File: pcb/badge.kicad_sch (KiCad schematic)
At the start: 17 parts, among them J1 USB_C_Receptacle_USB2.0_16P, U1 ESP32-C3-WROOM-02, U2 AMS1117-3.3

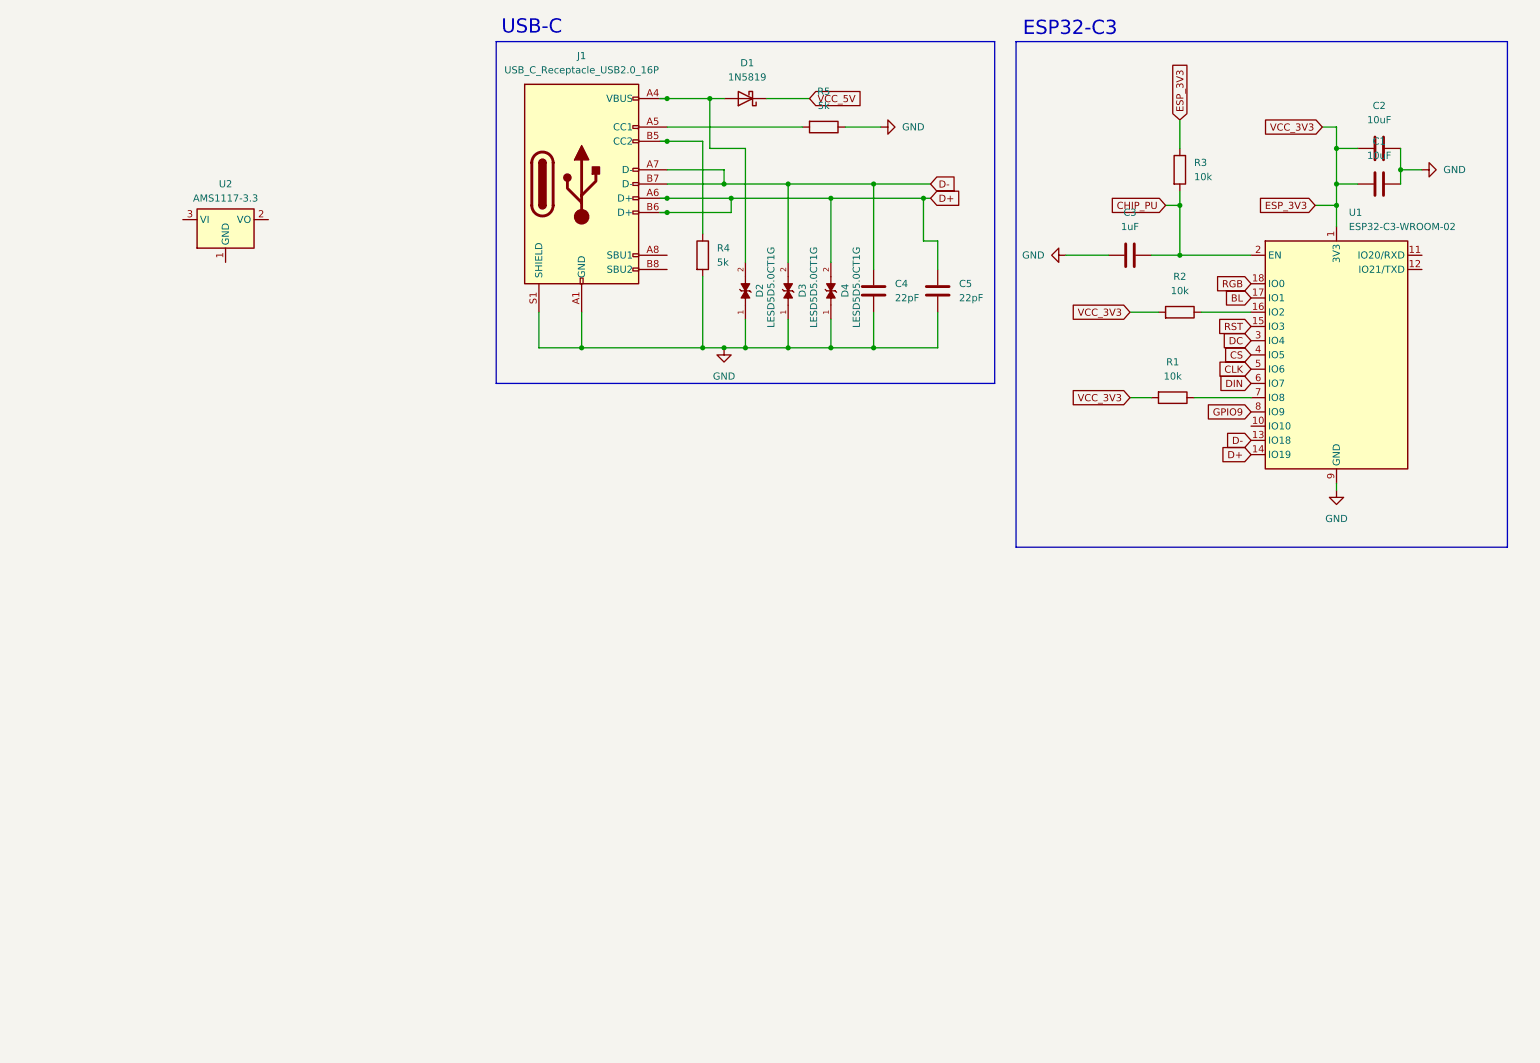
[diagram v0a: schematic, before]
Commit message: Made symbol for GDEY0213F51
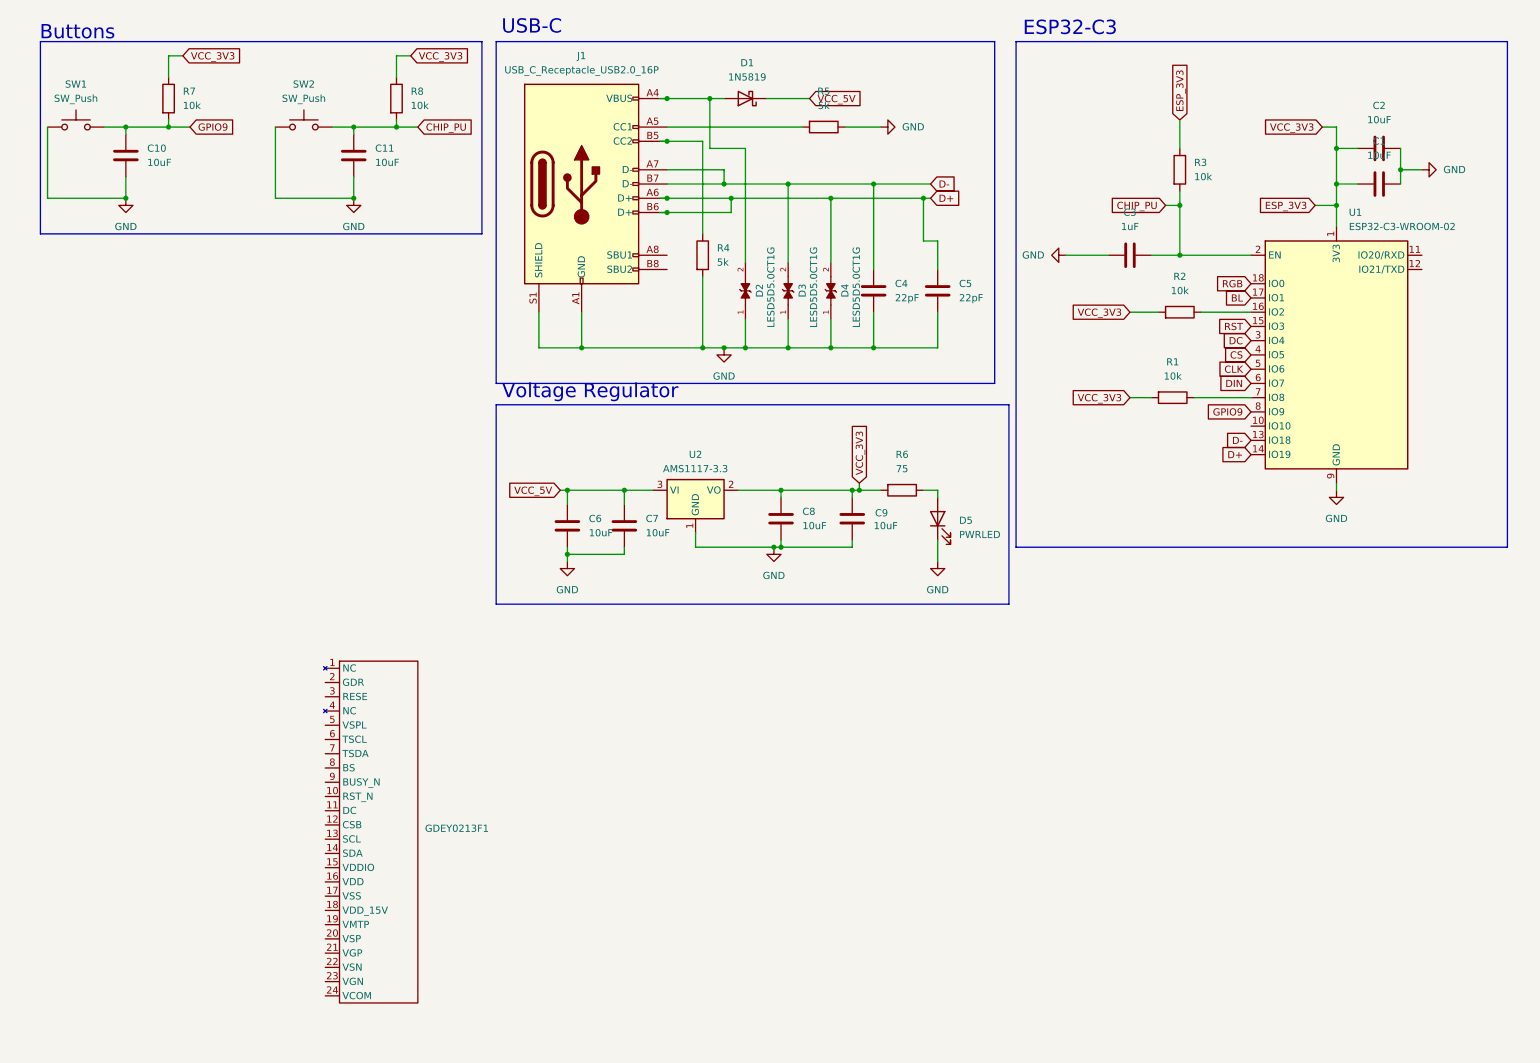
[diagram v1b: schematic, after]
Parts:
- added C10, C11, C6, C7, C8, C9: 10uF, symbol Device:C
- added D5: PWRLED, symbol Device:LED
- added GDEY0213F1: ~, symbol GDEY0213F51:GDEY0213F51
- added R6: 75, symbol Device:R
- added R7, R8: 10k, symbol Device:R
- added SW1, SW2: SW_Push, symbol Switch:SW_Push
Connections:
- net CHIP_PU: now also C11.1, R8.2, SW2.2
- net ESP_3V3: now also U2.2 (VO), C8.1, C9.1, R6.2, R7.1, R8.1
- net GND: now also U2.1 (GND), C10.2, C11.2, C6.2, C7.2, C8.2, C9.2, D5.1 (K), SW1.1, SW2.1
- net GPIO9: now also C10.1, R7.2, SW1.2
- net VCC_5V: now also U2.3 (VI), C6.1, C7.1
- new net: D5.2 (A), R6.1
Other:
- note added: "Buttons"
- note added: "Voltage Regulator"
- moved on the sheet: U2

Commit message: Began changing to rp2040
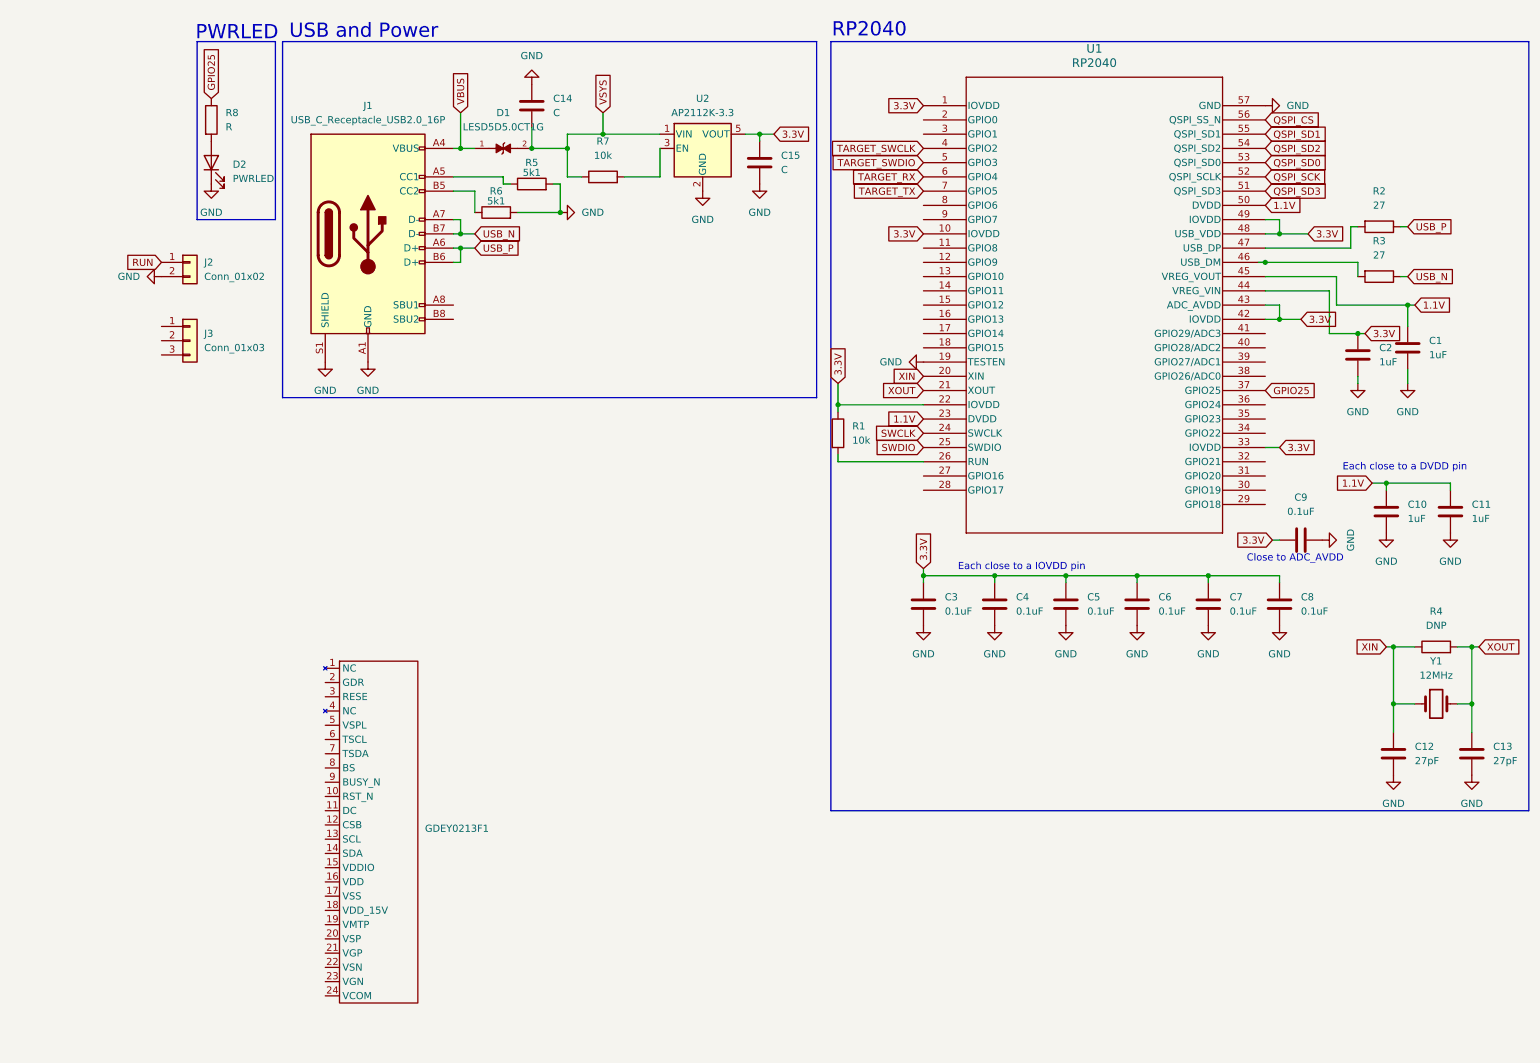
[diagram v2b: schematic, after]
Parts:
- removed D1: 1N5819, Diode_THT:D_DO-41_SOD81_P10.16mm_Horizontal, symbol Diode:1N5819
- removed D2, D3, D4: LESD5D5.0CT1G, LESD5D5.0CT1G:TVS_LESD5D5.0CT1G, symbol LESD5D5.0CT1G:LESD5D5.0CT1G
- removed D5: PWRLED, symbol Device:LED
- removed SW1, SW2: SW_Push, symbol Switch:SW_Push
- removed U1: ESP32-C3-WROOM-02, RF_Module:ESP32-C3-WROOM-02, symbol RF_Module:ESP32-C3-WROOM-02
- removed U2: AMS1117-3.3, Package_TO_SOT_SMD:SOT-223-3_TabPin2, symbol Regulator_Linear:AMS1117-3.3
- added C12, C13: 27pF, symbol Device:C
- added C14, C15: C, symbol Device:C
- added D1: LESD5D5.0CT1G, LESD5D5.0CT1G:TVS_LESD5D5.0CT1G, symbol LESD5D5.0CT1G:LESD5D5.0CT1G
- added D2: PWRLED, symbol Device:LED
- added J2: Conn_01x02, symbol Connector_Generic:Conn_01x02
- added J3: Conn_01x03, symbol Connector_Generic:Conn_01x03
- added U1: RP2040, IC57_RP2040, symbol RP2040:RP2040
- added U2: AP2112K-3.3, Package_TO_SOT_SMD:SOT-23-5, symbol Regulator_Linear:AP2112K-3.3
- added Y1: 12MHz, symbol Device:Crystal
- C1, C10, C11, C2: value 10uF -> 1uF
- C3: value 1uF -> 0.1uF
- C4, C5: value 22pF -> 0.1uF
- C6, C7, C8, C9: value 10uF -> 0.1uF
- R2, R3: value 10k -> 27
- R4: value 5k -> DNP
- R5: value 5k -> 5k1
- R6: value 75 -> 5k1
- R8: value 10k -> R
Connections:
- net VCC_5V is gone; now on net 3.3V: C6.1, C7.1
- net GND: now also C1.2, C3.2, R5.2, R6.2, C12.2, C13.2, C14.1, C15.2, D2.1 (K), J2.2 (Pin_2), U1.19 (TESTEN), U1.57 (GND), U2.2 (GND); no longer C1.1, C3.1, R4.2, R5.1
- net at J1.A5 (CC1): now also R5.1; no longer R5.2
- net VBUS: now reaches J1.A4 (VBUS), J1.A9 (VBUS), J1.B4 (VBUS), J1.B9 (VBUS)
- net VBUS: now also D1.1
- net at R6.1: now also J1.B5 (CC2)
- net XIN: now reaches R4.1
- net XIN: now also C12.1, U1.20 (XIN), Y1.1; no longer J1.B5 (CC2)
- net 3.3V: now reaches R1.1
- net 3.3V: now also C2.1, C3.1, C4.1, C5.1, C8.1, C9.1, C15.1, U1.1 (IOVDD), U1.10 (IOVDD), U1.22 (IOVDD), U1.33 (IOVDD), U1.42 (IOVDD), U1.43 (ADC_AVDD), U1.44 (VREG_VIN), U1.48 (USB_VDD), U1.49 (IOVDD), U2.5 (VOUT)
- net USB_P: now reaches R2.1
- net USB_P: now also J1.A6 (D+), J1.B6 (D+)
- removed net CHIP_PU: C11.1, C3.2, R3.2, R8.2
- removed net D+: C5.1, J1.A6 (D+), J1.B6 (D+)
- net D- renamed USB_N
- net USB_N: now also R3.1; no longer C4.1
- removed net ESP_3V3: C1.2, C2.1, C8.1, C9.1, R1.2, R2.2, R3.1, R6.2, R7.1, R8.1
- net GPIO9: no longer names the net of R7.2
- net GPIO9: now also U2.3 (EN); no longer C10.1
- new net: R1.2, U1.26 (RUN)
- new net: R3.2, U1.46 (USB_DM)
- new net: R2.2, U1.47 (USB_DP)
- new net: D2.2 (A), R8.2
- new net 1.1V: C1.1, C10.1, C11.1, U1.23 (DVDD), U1.45 (VREG_VOUT), U1.50 (DVDD)
- new net GPIO25: R8.1, U1.37 (GPIO25)
- new net QSPI_CS: U1.56 (QSPI_SS_N)
- new net QSPI_SCK: U1.52 (QSPI_SCLK)
- new net QSPI_SD0: U1.53 (QSPI_SD0)
- new net QSPI_SD1: U1.55 (QSPI_SD1)
- new net QSPI_SD2: U1.54 (QSPI_SD2)
- new net QSPI_SD3: U1.51 (QSPI_SD3)
- new net RUN: J2.1 (Pin_1)
- new net SWCLK: U1.24 (SWCLK)
- new net SWDIO: U1.25 (SWDIO)
- new net TARGET_RX: U1.6 (GPIO4)
- new net TARGET_SWCLK: U1.4 (GPIO2)
- new net TARGET_SWDIO: U1.5 (GPIO3)
- new net TARGET_TX: U1.7 (GPIO5)
- new net VSYS: C14.2, D1.2, R7.1, U2.1 (VIN)
- new net XOUT: C13.1, R4.2, U1.21 (XOUT), Y1.2
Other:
- note added: "Close to ADC_AVDD"
- note added: "Each close to a DVDD pin"
- note added: "Each close to a IOVDD pin"
- note added: "PWRLED"
- note added: "RP2040"
- note added: "USB and Power"
- note removed: "Buttons"
- note removed: "ESP32-C3"
- note removed: "USB-C"
- note removed: "Voltage Regulator"

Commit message: Beginning to get footprints
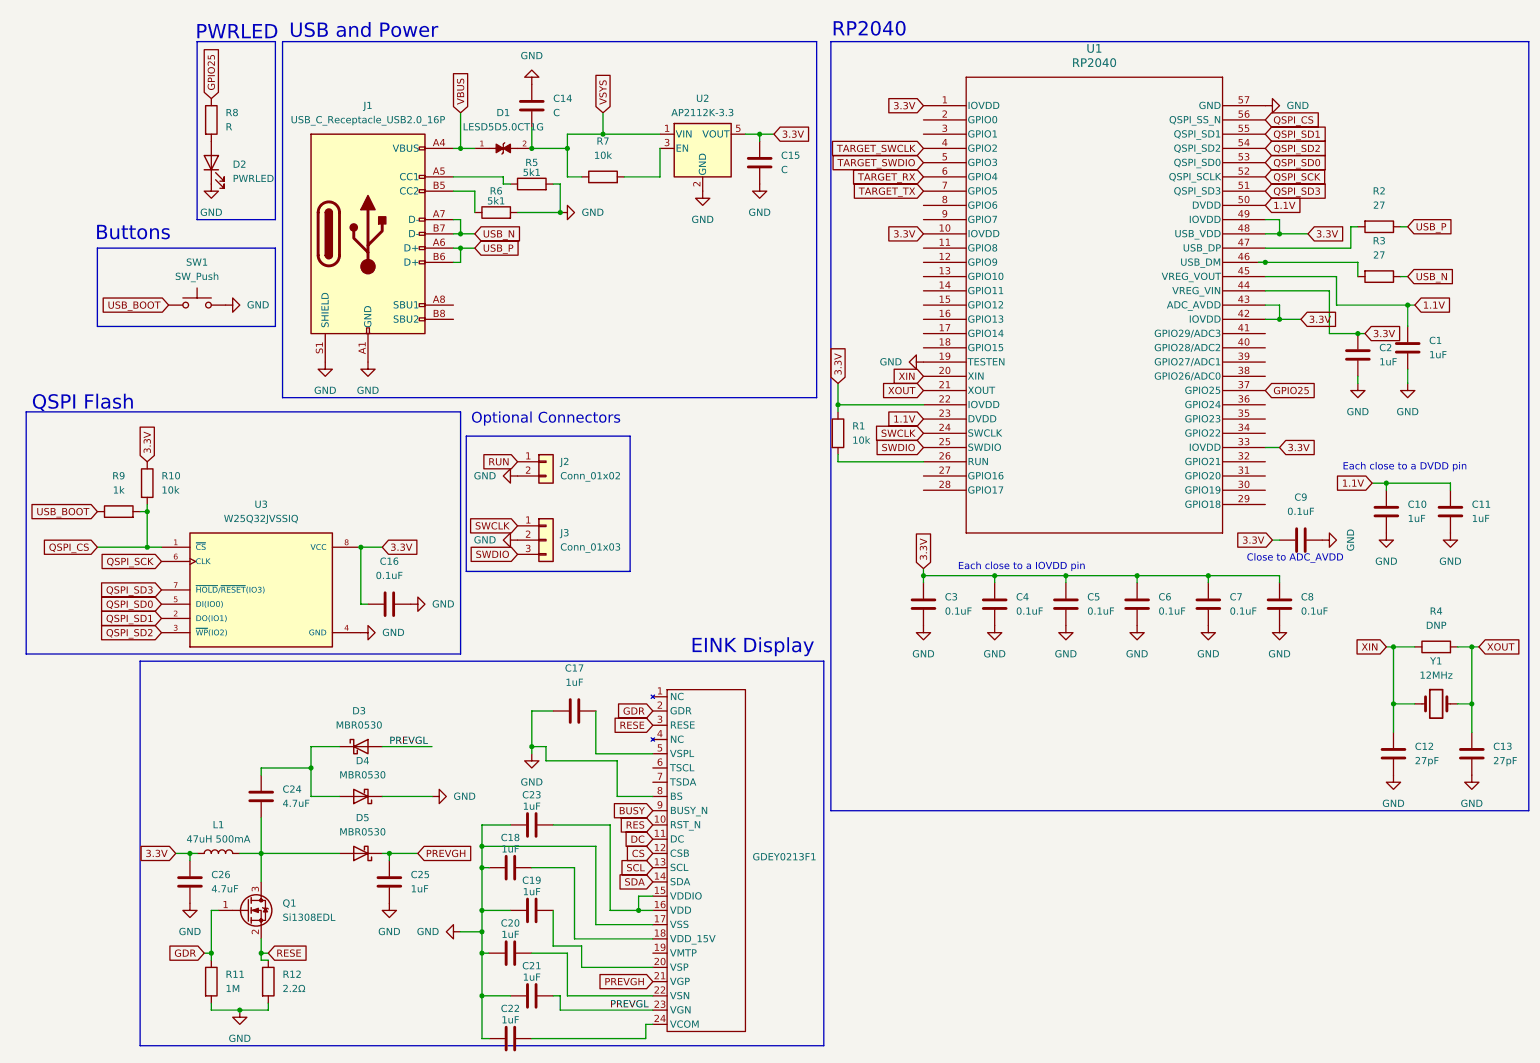
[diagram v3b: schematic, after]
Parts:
- added C16: 0.1uF, symbol Device:C
- added C17, C18, C19, C20, C21, C22, C23, C25: 1uF, symbol Device:C
- added C24, C26: 4.7uF, symbol Device:C
- added D3, D4, D5: MBR0530, Diode_SMD:D_SOD-123, symbol Diode:MBR0530
- added L1: 47uH 500mA, symbol Device:L
- added Q1: Si1308EDL, Package_TO_SOT_SMD:SOT-323_SC-70, symbol Transistor_FET:Si1308EDL
- added R10: 10k, symbol Device:R
- added R11: 1M, symbol Device:R
- added R12: 2.2Ω, symbol Device:R
- added R9: 1k, symbol Device:R
- added SW1: SW_Push, symbol Switch:SW_Push
- added U3: W25Q32JVSSIQ, W25Q32JVSSIQ:SOIC127P790X216-8N, symbol W25Q32JVSSIQ:W25Q32JVSSIQ
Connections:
- net 3.3V: now also C16.1, C26.1, L1.1, R10.1, U3.8 (VCC)
- net GND: now also GDEY0213F1.17 (VSS), GDEY0213F1.8 (BS), J3.2 (Pin_2), C16.2, C17.1, C18.1, C19.1, C20.1, C21.1, C22.1, C23.1, C25.2, C26.2, D4.1 (K), R11.2, R12.2, SW1.2, U3.4 (GND)
- net QSPI_CS: now also R10.2, R9.2, U3.1 (~{CS})
- net QSPI_SCK: now also U3.6 (CLK)
- net QSPI_SD0: now also U3.5 (DI(IO0))
- net QSPI_SD1: now also U3.2 (DO(IO1))
- net QSPI_SD2: now also U3.3 (~{WP}(IO2))
- net QSPI_SD3: now also U3.7 (~{HOLD}/~{RESET}(IO3))
- net SWCLK: now also J3.1 (Pin_1)
- net SWDIO: now also J3.3 (Pin_3)
- net RES: now reaches GDEY0213F1.10 (RST_N)
- net DC: now reaches GDEY0213F1.11 (DC)
- net CS: now reaches GDEY0213F1.12 (CSB)
- net SCL: now reaches GDEY0213F1.13 (SCL)
- net SDA: now reaches GDEY0213F1.14 (SDA)
- net at GDEY0213F1.15 (VDDIO): now also GDEY0213F1.16 (VDD), C23.2
- net at GDEY0213F1.18 (VDD_15V): now also C18.2
- net GDR: now reaches GDEY0213F1.2 (GDR)
- net GDR: now also Q1.1 (G), R11.1
- net at GDEY0213F1.20 (VSP): now also C19.2
- net PREVGH: now reaches GDEY0213F1.21 (VGP)
- net PREVGH: now also C25.1, D5.1 (K)
- net at GDEY0213F1.22 (VSN): now also C20.2
- net PREVGL: now reaches GDEY0213F1.23 (VGN)
- net PREVGL: now also C21.2, D3.2 (A)
- net at GDEY0213F1.24 (VCOM): now also C22.2
- net RESE: now reaches GDEY0213F1.3 (RESE)
- net RESE: now also Q1.2 (S), R12.1
- net at GDEY0213F1.5 (VSPL): now also C17.2
- net BUSY: now reaches GDEY0213F1.9 (BUSY_N)
- new net: C24.2, D5.2 (A), L1.2, Q1.3 (D)
- new net: C24.1, D3.1 (K), D4.2 (A)
- new net USB_BOOT: R9.1, SW1.1
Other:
- note added: "Buttons"
- note added: "EINK Display"
- note added: "Optional Connectors"
- note added: "QSPI Flash"
- company: (none) -> Hack Canada
- title: (none) -> Hack Canada Badge
- moved on the sheet: GDEY0213F1, J2, J3
